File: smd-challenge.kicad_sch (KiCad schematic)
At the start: 26 parts, among them J1 DX07S016JA1R1500, J2 Conn_01x05, U1 MIC5504-3.3YM5, U2 ATSAMD21E15B-M, Y1 ECS-160-18-33QZ-ADS-TR

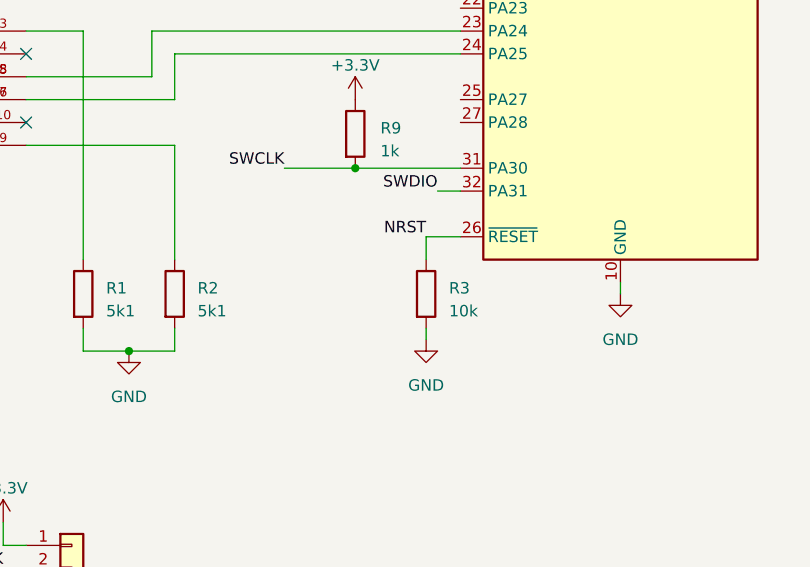
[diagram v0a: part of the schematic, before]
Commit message: /NRST should be connected to a pull-UP
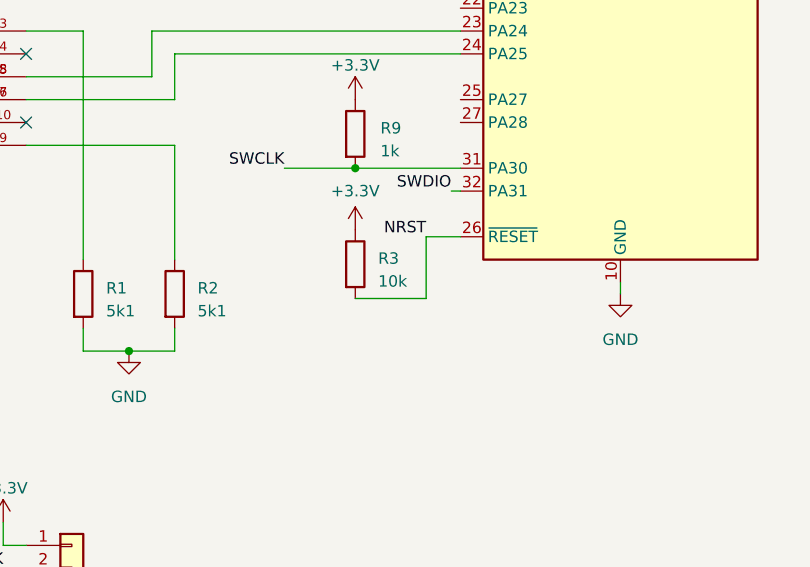
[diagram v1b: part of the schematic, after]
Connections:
- net +3V3: now also R3.1
- net GND: no longer R3.2
- net NRST: now also R3.2; no longer R3.1
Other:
- moved on the sheet: R3
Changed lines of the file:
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@@
+    (stroke (width 0) (type solid) (color 0 0 0 0))
+  )
+  (wire (pts (xy 106.68 130.81) (xy 106.68 137.668))
     (stroke (width 0) (type solid) (color 0 0 0 0))
   )
@@
     (stroke (width 0) (type solid) (color 0 0 0 0))
   )
-  (wire (pts (xy 106.68 133.35) (xy 106.68 130.81))
-    (stroke (width 0) (type solid) (color 0 0 0 0))
-  )
-  (wire (pts (xy 106.68 140.97) (xy 106.68 142.24))
+  (wire (pts (xy 106.68 137.668) (xy 98.806 137.668))
     (stroke (width 0) (type solid) (color 0 0 0 0))
   )
@@
     (stroke (width 0) (type solid) (color 0 0 0 0))
   )
-  (wire (pts (xy 107.95 125.73) (xy 110.49 125.73))
-    (stroke (width 0) (type solid) (color 0 0 0 0))
-  )
   (wire (pts (xy 109.22 25.4) (xy 120.65 25.4))
     (stroke (width 0) (type solid) (color 0 0 0 0))
   )
+  (wire (pts (xy 109.474 125.73) (xy 110.49 125.73))
+    (stroke (width 0) (type solid) (color 0 0 0 0))
+  )
   (wire (pts (xy 110.49 110.49) (xy 78.74 110.49))
     (stroke (width 0) (type solid) (color 0 0 0 0))
@@
     (effects (font (size 1.27 1.27)) (justify right bottom))
   )
-  (label "SWDIO" (at 107.95 125.73 180)
+  (label "SWDIO" (at 109.474 125.73 180)
     (effects (font (size 1.27 1.27)) (justify right bottom))
   )
@@
     (pin "1")
   )
+  (symbol (lib_id "power:+3.3V") (at 98.806 130.048 0) (unit 1)
+    (in_bom yes) (on_board yes)
+    (property "Reference" "#PWR?" (id 0) (at 98.806 133.858 0)
+      (effects (font (size 1.27 1.27)) hide)
+    )
+    (property "Value" "+3.3V" (id 1) (at 98.806 125.73 0))
+    (property "Footprint" "" (id 2) (at 98.806 130.048 0)
+      (effects (font (size 1.27 1.27)) hide)
+    )
+    (property "Datasheet" "" (id 3) (at 98.806 130.048 0)
+      (effects (font (size 1.27 1.27)) hide)
+    )
+    (pin "1")
+  )
   (symbol (lib_id "power:+3.3V") (at 130.81 24.13 0) (unit 1)
     (in_bom yes) (on_board yes)
@@
     (pin "1")
   )
-  (symbol (lib_id "power:GND") (at 106.68 142.24 0) (unit 1)
-    (in_bom yes) (on_board yes)
-    (property "Reference" "#PWR011" (id 0) (at 106.68 148.59 0)
-      (effects (font (size 1.27 1.27)) hide)
-    )
-    (property "Value" "GND" (id 1) (at 106.68 147.32 0))
-    (property "Footprint" "" (id 2) (at 106.68 142.24 0)
-      (effects (font (size 1.27 1.27)) hide)
-    )
-    (property "Datasheet" "" (id 3) (at 106.68 142.24 0)
-      (effects (font (size 1.27 1.27)) hide)
-    )
-    (pin "1")
-  )
   (symbol (lib_id "power:GND") (at 109.22 33.02 0) (unit 1)
     (in_bom yes) (on_board yes)
@@
     (pin "2")
   )
-  (symbol (lib_id "Device:R") (at 106.68 137.16 0) (unit 1)
-    (in_bom yes) (on_board yes)
-    (property "Reference" "R3" (id 0) (at 109.22 136.5249 0)
-      (effects (font (size 1.27 1.27)) (justify left))
-    )
-    (property "Value" "10k" (id 1) (at 109.22 139.0649 0)
-      (effects (font (size 1.27 1.27)) (justify left))
-    )
-    (property "Footprint" "Resistor_SMD:R_0603_1608Metric" (id 2) (at 104.902 137.16 90)
-      (effects (font (size 1.27 1.27)) hide)
-    )
-    (property "Datasheet" "~" (id 3) (at 106.68 137.16 0)
+  (symbol (lib_id "Device:R") (at 98.806 133.858 0) (unit 1)
+    (in_bom yes) (on_board yes)
+    (property "Reference" "R3" (id 0) (at 101.346 133.2229 0)
+      (effects (font (size 1.27 1.27)) (justify left))
+    )
+    (property "Value" "10k" (id 1) (at 101.346 135.7629 0)
+      (effects (font (size 1.27 1.27)) (justify left))
+    )
+    (property "Footprint" "Resistor_SMD:R_0603_1608Metric" (id 2) (at 97.028 133.858 90)
+      (effects (font (size 1.27 1.27)) hide)
+    )
+    (property "Datasheet" "~" (id 3) (at 98.806 133.858 0)
       (effects (font (size 1.27 1.27)) hide)
     )
@@
       (reference "#PWR010") (unit 1) (value "GND") (footprint "")
     )
-    (path "/716cafd2-d40a-40fe-9b33-eb5de5a50fe9"
-      (reference "#PWR011") (unit 1) (value "GND") (footprint "")
-    )
     (path "/25b9b85a-d356-4648-8c29-67ee15d554df"
       (reference "#PWR012") (unit 1) (value "GND") (footprint "")
@@
       (reference "#PWR0102") (unit 1) (value "+3.3V") (footprint "")
     )
+    (path "/4f4f7792-fe5c-4699-b9df-eec8103c48dc"
+      (reference "#PWR?") (unit 1) (value "+3.3V") (footprint "")
+    )
     (path "/c5fa86be-8e49-41ac-91b5-adef14ae477a"
